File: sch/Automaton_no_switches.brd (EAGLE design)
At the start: 100 x 69.8 mm, 24 parts, among them IC1 74LS595D, IC2 74LS595D, IC3 74LS595D, IC4 74LS595D, J1 POWER_JACKPTH

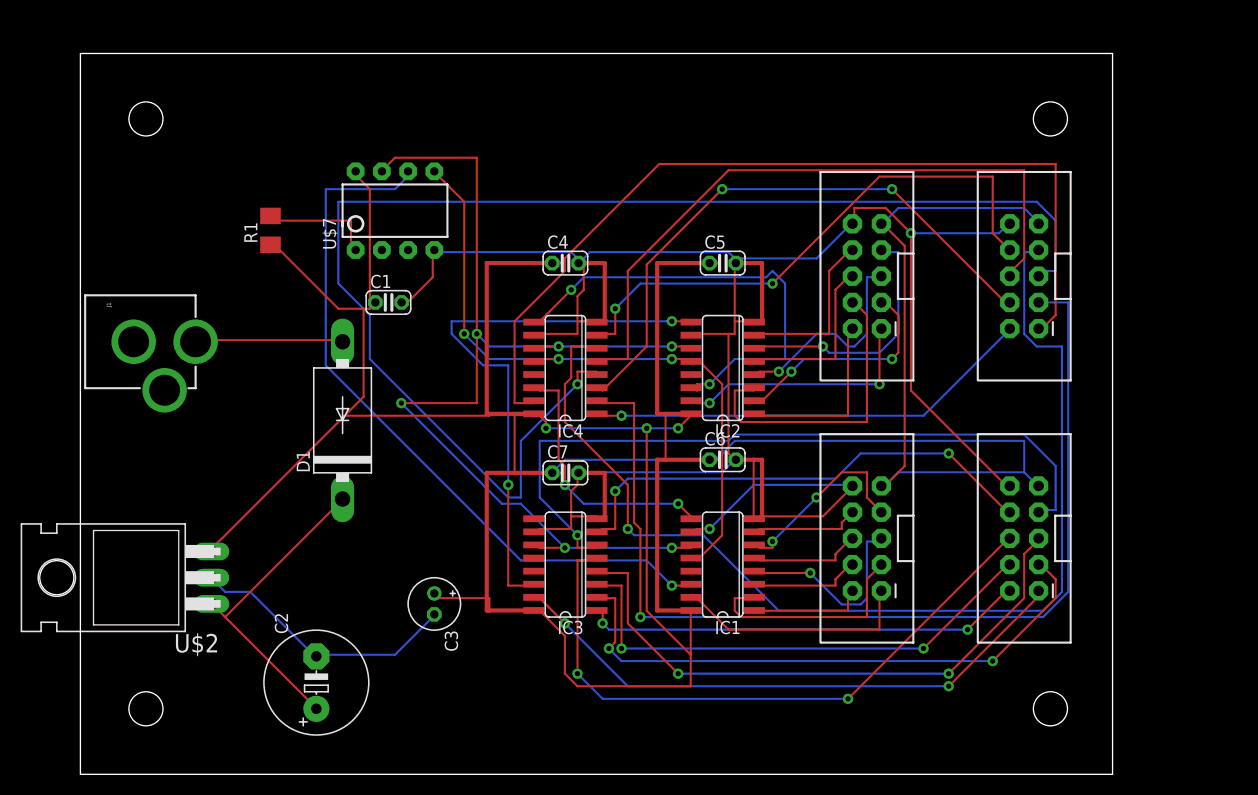
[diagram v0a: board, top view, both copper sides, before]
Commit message: added to schematic
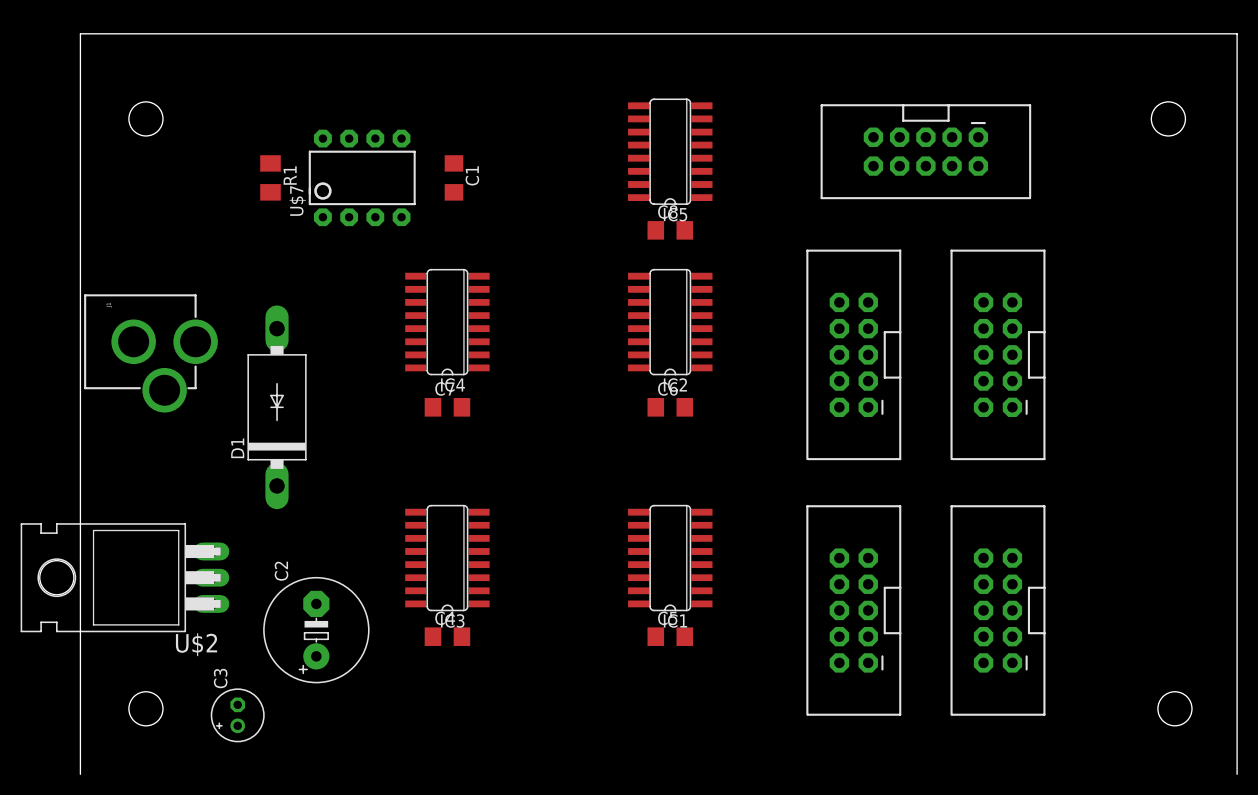
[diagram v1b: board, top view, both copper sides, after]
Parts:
- added C8: 0.1uf, resistor:C1206
- added IC5: 74LS595D, 74xx-us:SO16
- added U$1: AVR_SPI_PROG2LOCK, SparkFun:2X5-SHROUDED_LOCK
- C1, C4, C5, C6, C7: device resistor:C025-024X044 -> resistor:C1206
- R1: value 10k -> 100k
- moved C4 38.0 mm to (35.6, 13.3)
- moved C5 36.5 mm to (57.1, 13.3)
- moved C3 21.9 mm to (15.2, 5.71), turned to 90 degrees
- moved C1 13.6 mm to (36.2, 57.8), turned to 270 degrees
- moved C7 13.1 mm to (35.6, 35.6)
- moved IC4 12.3 mm to (35.6, 43.8)
- moved JP3 12.1 mm to (106.0, 6.35)
- moved IC3 11.4 mm to (35.6, 21.0)
- moved JP4 11.4 mm to (105.4, 63.5)
- moved U$5 8.03 mm to (88.9, 40.6)
- moved U$4 7.73 mm to (74.9, 40.6)
- moved U$3 7.43 mm to (88.9, 15.9)
- moved C6 7.18 mm to (57.1, 35.6)
- moved U$6 7.10 mm to (74.9, 15.9)
- moved IC2 6.75 mm to (57.1, 43.8)
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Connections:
- removed net 5V: C1.1, C3.+, C4.1, C5.1, C6.1, C7.1, R1.1, U$2.3, U$3.9, U$4.9, U$5.9, U$6.9, U$7.8
- removed net LED_RCLK: IC3.12
- removed net N$4: C2.-, C3.-, U$2.2
- new net LEDS_IC1_SER: IC1.14, IC5.9
- new net LED_33: IC5.15, U$1.1
- new net LED_34: IC5.1, U$1.2
- new net LED_35: IC5.2, U$1.3
- new net LED_36: IC5.3, U$1.4
- new net LED_37: IC5.4, U$1.5
- new net LED_38: IC5.5, U$1.6
- new net LED_39: IC5.6, U$1.7
- new net LED_40: IC5.7, U$1.8
- net GND: now also C2.-, C3.-, C8.2, IC1.13, IC2.13, IC3.13, IC4.13, IC5.13, IC5.8, J1.GND, U$1.10, U$2.2; no longer IC1.10, IC2.10, IC3.10, IC4.10
- net LEDS_RCLK: now also IC3.12, IC5.12
- net LEDS_SER: now also IC5.14; no longer IC1.14
- net LEDS_SRCLK: now also IC5.11
- net VCC: now also C1.1, C3.+, C4.1, C5.1, C6.1, C7.1, C8.1, IC1.10, IC2.10, IC3.10, IC4.10, IC5.10, IC5.16, R1.1, U$1.9, U$2.3, U$3.9, U$4.9, U$5.9, U$6.9, U$7.8
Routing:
- net 5V: track 292.9 -> 0.00 mm
- net GND: track 230.0 -> 0.00 mm, vias 2 -> 0
- net LED_21: track 130.3 -> 0.00 mm, vias 1 -> 0
- net LED_23: track 106.5 -> 0.00 mm, vias 1 -> 0
- net LEDS_SRCLK: track 101.9 -> 0.00 mm, vias 6 -> 0
- net LED_19: track 98.0 -> 0.00 mm, vias 1 -> 0
- net LED_17: track 86.2 -> 0.00 mm
- net LED_7: track 71.5 -> 0.00 mm, vias 1 -> 0
- net LEDS_SER: track 70.3 -> 0.00 mm, vias 1 -> 0
- net VCC: track 68.2 -> 0.00 mm, vias 3 -> 0
- net LEDS_RCLK: track 65.4 -> 0.00 mm, vias 3 -> 0
- net LED_22: track 64.8 -> 0.00 mm
- net LED_6: track 62.3 -> 0.00 mm, vias 2 -> 0
- net LED_5: track 57.7 -> 0.00 mm, vias 2 -> 0
- net LED_20: track 57.3 -> 0.00 mm, vias 2 -> 0
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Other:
- board size 100 x 69.8 mm -> 112.1 x 71.7 mm

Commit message: board passes batchpcb's DRC now
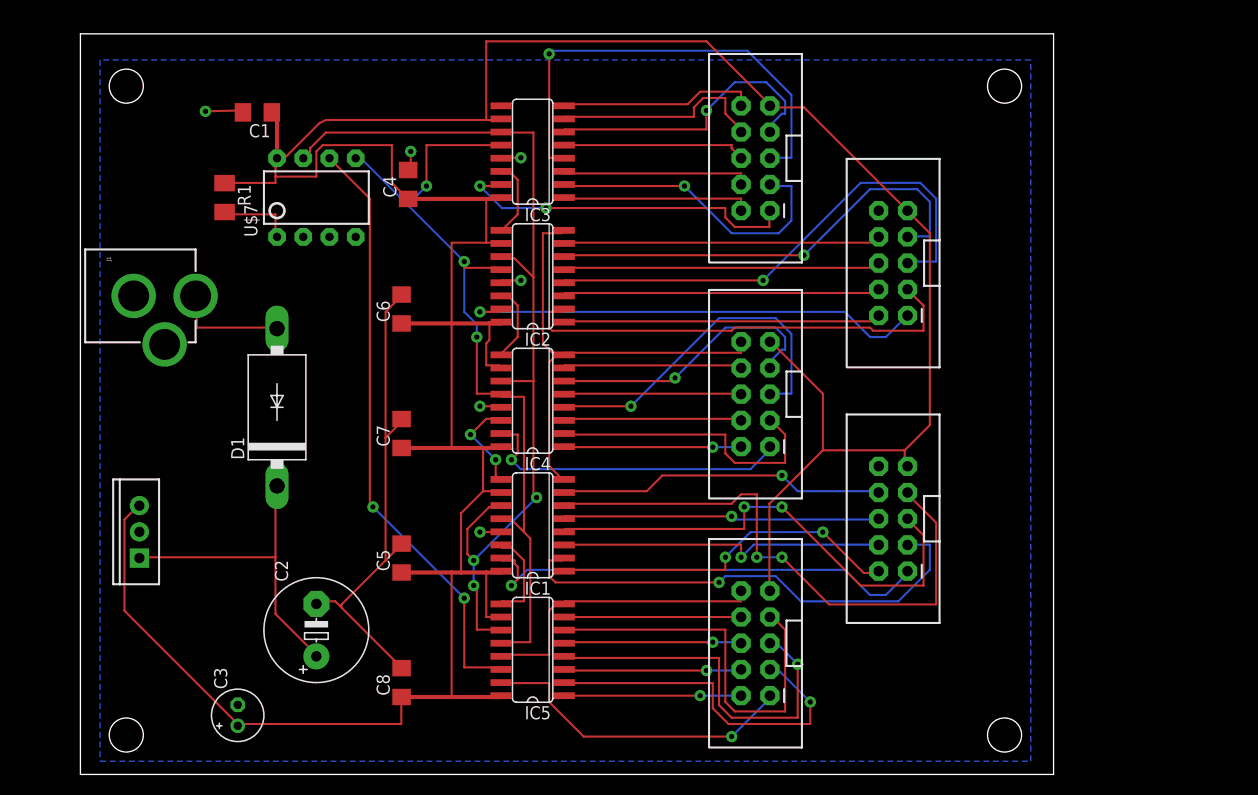
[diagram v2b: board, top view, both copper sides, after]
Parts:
- removed U$2: LM323, MyLib:TO220H
- added IC6: (no value), SparkFun-PowerIC:TO220-IGO
- moved JP2 60.4 mm to (4.45, 66.7)
- moved JP1 59.7 mm to (4.45, 3.81)
- moved C8 51.0 mm to (31.1, 8.89), turned to 90 degrees
- moved U$1 50.4 mm to (65.4, 12.7), turned to 180 degrees
- moved IC5 50.1 mm to (43.8, 12.1)
- moved U$3 49.7 mm to (65.4, 59.7)
- moved C4 44.0 mm to (31.8, 57.1), turned to 90 degrees
- moved IC3 40.2 mm to (43.8, 60.3)
- moved C6 27.7 mm to (31.1, 45.1), turned to 90 degrees
- moved C5 27.1 mm to (31.1, 21.0), turned to 90 degrees
- moved U$5 23.8 mm to (65.4, 36.8)
- moved C1 20.1 mm to (17.1, 64.1), turned to 180 degrees
- moved JP3 16.7 mm to (89.5, 3.81)
- moved JP4 16.2 mm to (89.5, 66.7)
- moved IC2 14.1 mm to (43.8, 48.3)
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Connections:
- net GND: now also IC6.GND, J1.GNDBREAK; no longer U$2.2
- net N$1: now also IC6.IN; no longer U$2.1
- net VCC: now also IC6.OUT; no longer U$2.3
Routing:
- net VCC: track 0.00 -> 334.9 mm
- net GND: track 0.00 -> 158.1 mm, vias 0 -> 6
- net LEDS_SRCLK: track 0.00 -> 91.4 mm, vias 0 -> 3
- net LEDS_RCLK: track 0.00 -> 80.4 mm, vias 0 -> 3
- net LEDS_SER: track 0.00 -> 58.4 mm, vias 0 -> 2
- net LED_31: track 0.00 -> 56.5 mm, vias 0 -> 2
- net LED_13: track 0.00 -> 49.7 mm, vias 0 -> 1
- net LED_29: track 0.00 -> 47.4 mm, vias 0 -> 2
- net LED_27: track 0.00 -> 47.4 mm, vias 0 -> 1
- net LED_9: track 0.00 -> 45.5 mm, vias 0 -> 1
- net LED_25: track 0.00 -> 45.4 mm, vias 0 -> 1
- net LED_5: track 0.00 -> 45.1 mm, vias 0 -> 1
- net LED_11: track 0.00 -> 44.4 mm
- net LED_15: track 0.00 -> 44.2 mm, vias 0 -> 1
- net LED_39: track 0.00 -> 38.7 mm
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- added copper zone on layer 16, net GND
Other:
- board size 112.1 x 71.7 mm -> 94.3 x 71.8 mm

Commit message: reduced the board size, added some parts to the schematic and board (power switch, breakout for unused MCU pins, power LED)
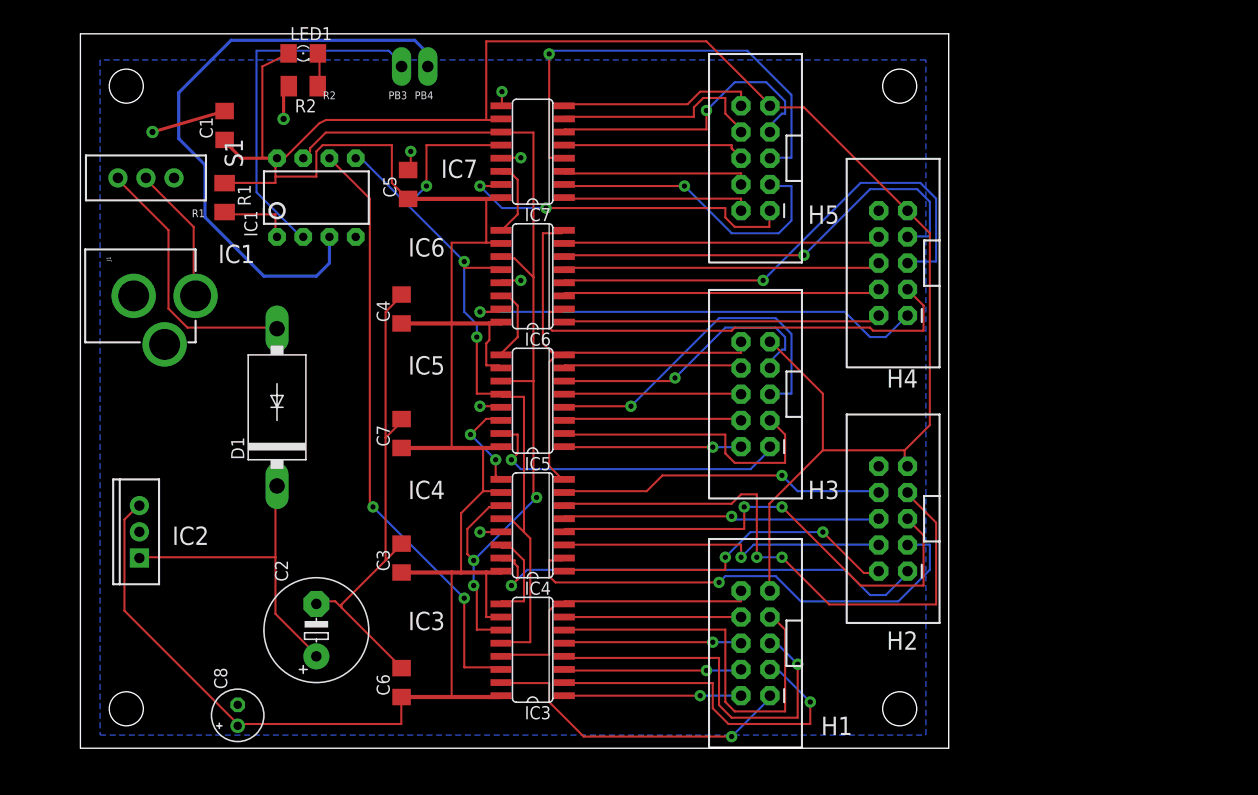
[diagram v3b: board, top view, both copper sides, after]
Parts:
- removed JP1, JP3, JP4: STAND-OFF, SparkFun-Electromechanical:STAND-OFF
- removed U$7: ATTINY85DIP8, *Personal Library:DIP08
- added HOLE2, HOLE3, HOLE4: STAND-OFF, SparkFun-Electromechanical:STAND-OFF
- added IC7: 74LS595D, 74xx-us:SO16
- added IO1: (no value), SparkFun-Connectors:1X02_LONGPADS
- added LED1: (no value), led:1206
- added R2: 330, resistor:M1206
- added S1: (no value), SparkFun-Electromechanical:SWITCH-SPDT_LOCK.007S
- C3: value 10uf -> 0.1uf; device rcl:E2-5 -> resistor:C1206
- C8: value 0.1uf -> 10uf; device resistor:C1206 -> rcl:E2-5
- IC1: value 74LS595D -> ATTINY85DIP8; device 74xx-us:SO16 -> *Personal Library:DIP08
- IC2: value 74LS595D -> LM323T; device 74xx-us:SO16 -> SparkFun-PowerIC:TO220-IGO
- IC6: value (none) -> 74LS595D; device SparkFun-PowerIC:TO220-IGO -> 74xx-us:SO16
- moved IC3 48.3 mm to (43.8, 12.1)
- moved IC2 45.4 mm to (5.71, 23.5)
- moved IC6 45.4 mm to (43.8, 48.3)
- moved IC1 38.0 mm to (22.9, 55.9), turned to 0 degrees
- moved C5 36.2 mm to (31.8, 57.1)
- moved C6 36.2 mm to (31.1, 8.89)
- moved IC5 24.1 mm to (43.8, 36.2)
- moved C3 22.0 mm to (31.1, 21.0)
- moved C8 16.2 mm to (15.2, 5.71)
- moved C4 12.1 mm to (31.1, 45.1)
- moved IC4 12.1 mm to (43.8, 24.1)
- moved C1 3.42 mm to (14.0, 62.9), turned to 90 degrees
- renumbered JP2 to HOLE1, U$1 to H1, U$3 to H5, U$4 to H4, U$5 to H3, U$6 to H2
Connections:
- removed net LEDS_IC1_SER: IC1.14, IC5.9
- removed net LEDS_IC2_SER: IC1.9, IC4.14
- removed net LEDS_IC3_SER: IC2.14, IC4.9
- new net LEDS_IC5_SER: IC4.9, IC5.14
- new net LEDS_IC6_SER: IC5.9, IC6.14
- new net LEDS_IC7_SER: IC6.9, IC7.14
- new net N$4: D1.A, S1.3
- new net N$5: LED1.C, R2.1
- new net PB3: IC1.2, IO1.1
- new net PB4: IC1.3, IO1.2
- net GND: now also C3.2, C8.-, IC1.4, IC2.GND, IC6.13, IC6.8, IC7.13, IC7.8, IC7.9, R2.2; no longer C3.-, C8.2, IC1.13, IC1.8, IC2.13, IC2.8, IC6.GND, U$7.4
- net LEDS_IC4_SER: now also IC3.9, IC4.14; no longer IC2.9, IC3.14
- net LEDS_RCLK: now also IC1.5, IC6.12, IC7.12; no longer IC1.12, IC2.12, U$7.5
- net LEDS_SER: now also IC1.6, IC3.14; no longer IC5.14, U$7.6
- net LEDS_SRCLK: now also IC1.7, IC6.11, IC7.11; no longer IC1.11, IC2.11, U$7.7
- net LED_1: now also IC7.15; no longer IC3.15
- net LED_10: now also IC6.1; no longer IC2.1
- net LED_11: now also IC6.2; no longer IC2.2
- net LED_12: now also IC6.3; no longer IC2.3
- net LED_13: now also IC6.4; no longer IC2.4
- net LED_14: now also IC6.5; no longer IC2.5
- net LED_15: now also IC6.6; no longer IC2.6
- net LED_16: now also IC6.7; no longer IC2.7
- net LED_17: now also IC5.15; no longer IC4.15
- net LED_18: now also IC5.1; no longer IC4.1
- net LED_19: now also IC5.2; no longer IC4.2
- net LED_2: now also IC7.1; no longer IC3.1
- net LED_20: now also IC5.3; no longer IC4.3
- net LED_21: now also IC5.4; no longer IC4.4
- net LED_22: now also IC5.5; no longer IC4.5
- net LED_23: now also IC5.6; no longer IC4.6
- net LED_24: now also IC5.7; no longer IC4.7
- net LED_25: now also IC4.15; no longer IC1.15
- net LED_26: now also IC4.1; no longer IC1.1
- net LED_27: now also IC4.2; no longer IC1.2
- net LED_28: now also IC4.3; no longer IC1.3
- net LED_29: now also IC4.4; no longer IC1.4
- net LED_3: now also IC7.2; no longer IC3.2
- net LED_30: now also IC4.5; no longer IC1.5
- net LED_31: now also IC4.6; no longer IC1.6
- net LED_32: now also IC4.7; no longer IC1.7
- net LED_33: now also IC3.15; no longer IC5.15
- net LED_34: now also IC3.1; no longer IC5.1
- net LED_35: now also IC3.2; no longer IC5.2
- net LED_36: now also IC3.3; no longer IC5.3
- net LED_37: now also IC3.4; no longer IC5.4
- net LED_38: now also IC3.5; no longer IC5.5
- net LED_39: now also IC3.6; no longer IC5.6
- net LED_4: now also IC7.3; no longer IC3.3
- net LED_40: now also IC3.7; no longer IC5.7
- net LED_5: now also IC7.4; no longer IC3.4
- net LED_6: now also IC7.5; no longer IC3.5
- net LED_7: now also IC7.6; no longer IC3.6
- net LED_8: now also IC7.7; no longer IC3.7
- net LED_9: now also IC6.15; no longer IC2.15
- net N$1: now also IC2.IN; no longer IC6.IN
- net N$2: now also IC1.1; no longer U$7.1
- net N$3: now also S1.2; no longer D1.A
- net VCC: now also C3.1, C8.+, IC1.8, IC2.OUT, IC6.10, IC6.16, IC7.10, IC7.16, LED1.A; no longer C3.+, C8.1, IC1.10, IC1.16, IC2.10, IC2.16, IC6.OUT, U$7.8
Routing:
- net PB4: track 0.00 -> 58.6 mm
- net PB3: track 0.00 -> 35.2 mm
- net N$4: track 0.00 -> 26.0 mm
- net VCC: track 334.9 -> 348.9 mm
- net LEDS_IC1_SER: track 9.31 -> 0.00 mm
- net LEDS_IC5_SER: track 0.00 -> 9.25 mm, vias 0 -> 2
- net LEDS_IC2_SER: track 9.25 -> 0.00 mm, vias 2 -> 0
- net GND: track 158.1 -> 166.5 mm, vias 6 -> 8
- net LEDS_IC7_SER: track 0.00 -> 7.62 mm
- net LEDS_IC6_SER: track 0.00 -> 7.44 mm
- net LEDS_IC3_SER: track 7.44 -> 0.00 mm
- net N$5: track 0.00 -> 3.40 mm
- net N$3: track 11.0 -> 13.4 mm
- net LEDS_IC4_SER: track 7.62 -> 9.31 mm
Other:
- board size 94.3 x 71.8 mm -> 84.1 x 69.2 mm
- board text added: "H1"
- board text added: "H2"
- board text added: "H3"
- board text added: "H4"
- board text added: "H5"
- board text added: "IC1"
- board text added: "IC2"
- board text added: "IC3"
- board text added: "IC4"
- board text added: "IC5"
- board text added: "IC6"
- board text added: "IC7"
- board text added: "PB3"
- board text added: "PB4"
- board text added: "R1"
- board text added: "R2"
